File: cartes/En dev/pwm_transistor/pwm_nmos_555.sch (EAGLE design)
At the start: 15 parts, among them Q1 MOSFET-NCHANNELFQP30N06L, T1 2N2222

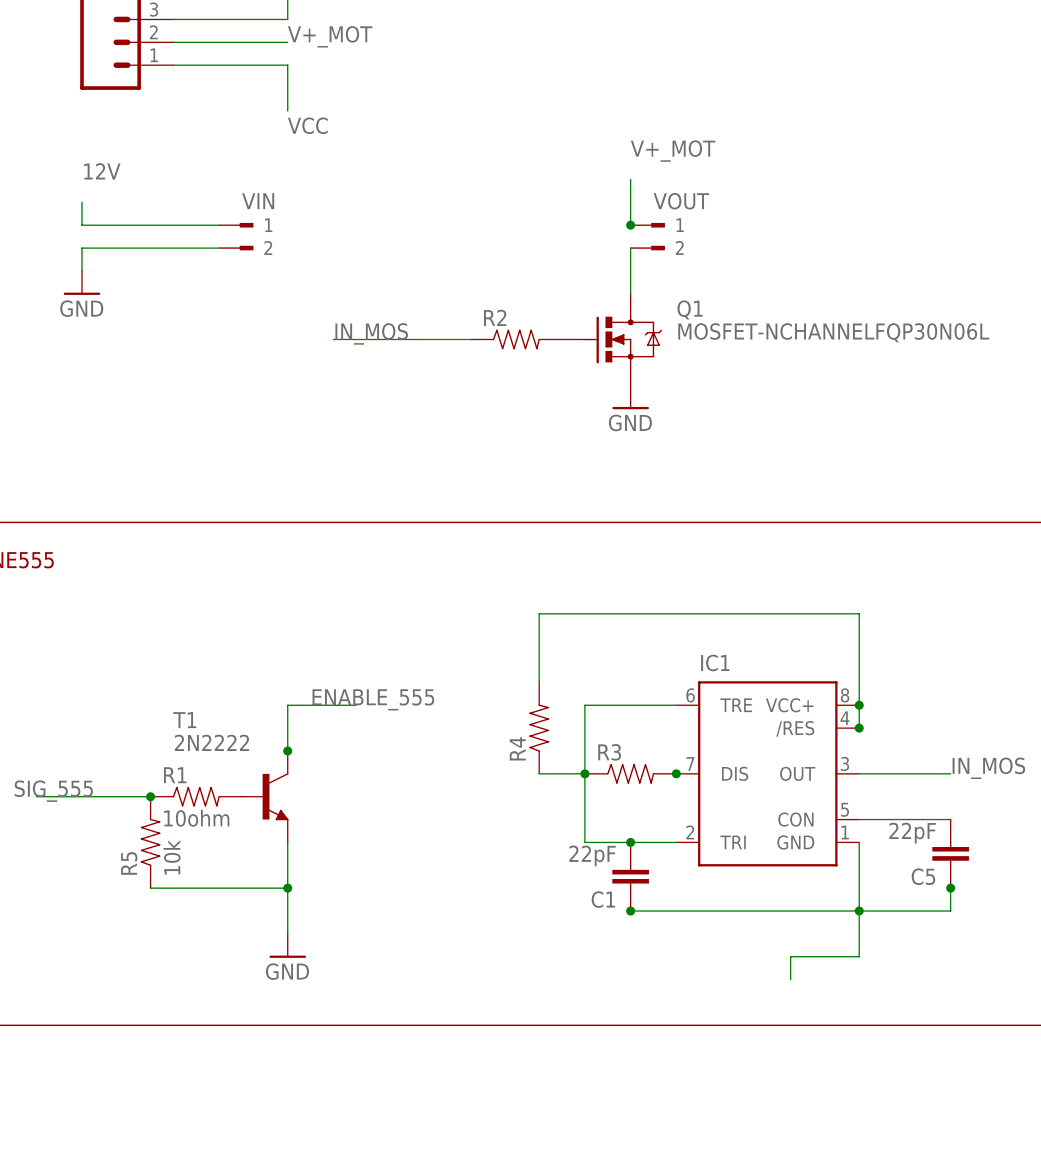
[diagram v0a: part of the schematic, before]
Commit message: carte mos pwm modifié
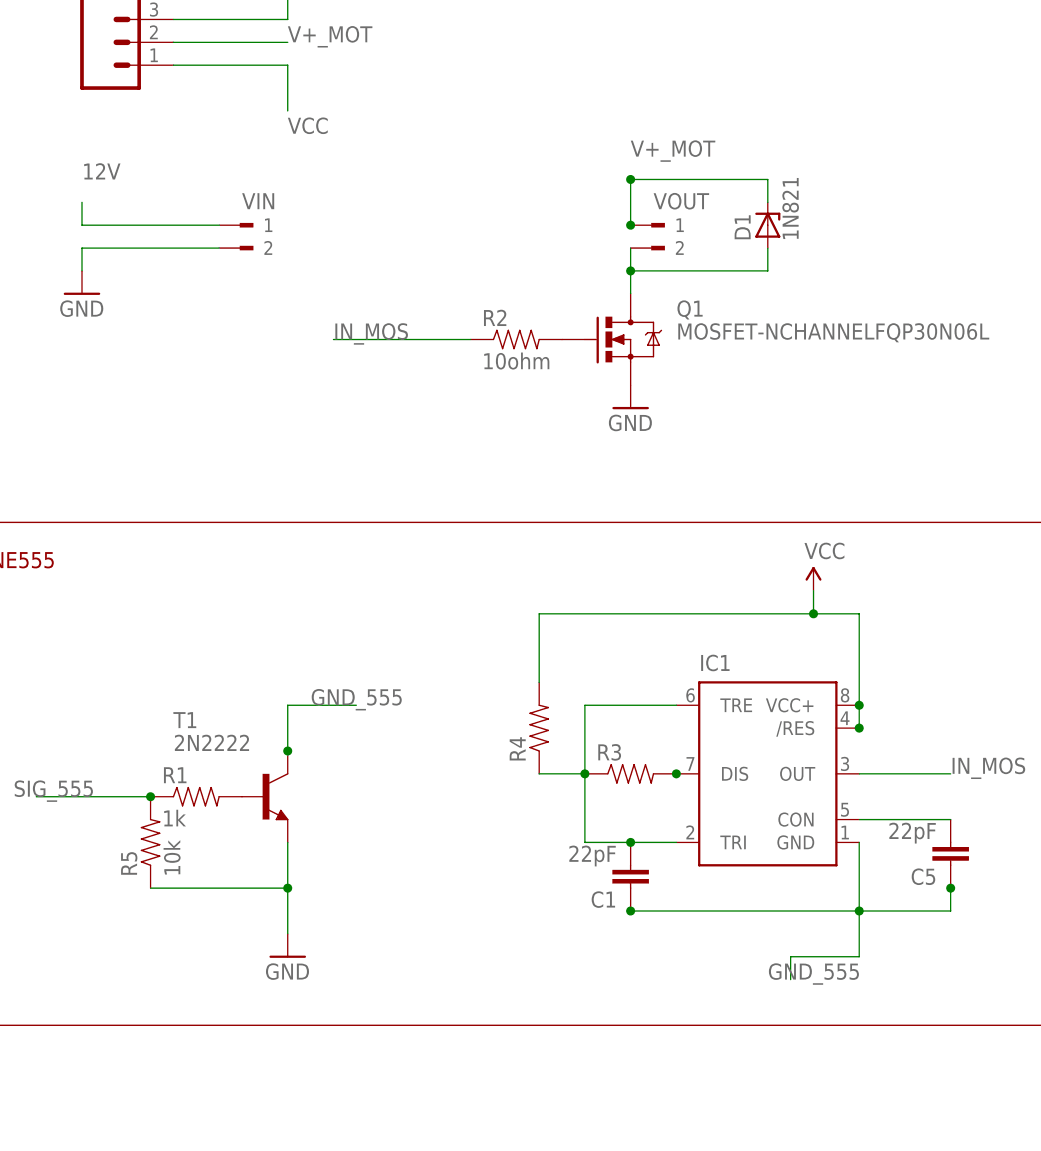
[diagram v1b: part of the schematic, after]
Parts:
- added D1: 1N821, diode:1N821
- R1: value 10ohm -> 1k
- R2: value (none) -> 10ohm
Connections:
- removed net ENABLE_555: T1.C
- removed net N$1: C1.1, C5.1, IC1.GND
- removed net N$7: IC1./RES, IC1.VCC+, R4.2
- new net GND_555: C1.1, C5.1, IC1.GND, T1.C
- net V+_MOT: now also D1.C
- net VCC: now also IC1./RES, IC1.VCC+, R4.2
- net VOUT: now also D1.A
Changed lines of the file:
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@@
 <part name="T1" library="adafruit" deviceset="2N2222" device=""/>
 <part name="INPUT" library="SparkFun-Electromechanical" deviceset="SMALL_SERVO" device="" value=""/>
-<part name="R1" library="SparkFun-Resistors" deviceset="RESISTOR" device="0805-RES" value="10ohm"/>
+<part name="R1" library="SparkFun-Resistors" deviceset="RESISTOR" device="0805-RES" value="1k"/>
 <part name="SUPPLY1" library="SparkFun-Aesthetics" deviceset="VCC" device=""/>
 <part name="GND1" library="SparkFun-Aesthetics" deviceset="GND" device=""/>
@@
 <part name="VIN" library="con-weidmueller-sl35" deviceset="90-2" device=""/>
 <part name="GND5" library="SparkFun-Aesthetics" deviceset="GND" device=""/>
-<part name="R2" library="SparkFun-Resistors" deviceset="RESISTOR" device="0805-RES"/>
+<part name="R2" library="SparkFun-Resistors" deviceset="RESISTOR" device="0805-RES" value="10ohm"/>
 <part name="SIGNAL" library="SparkFun-Connectors" deviceset="M03" device="PTH"/>
 <part name="R3" library="SparkFun-Resistors" deviceset="RESISTOR" device="0805-RES"/>
@@
 <part name="R5" library="SparkFun-Resistors" deviceset="RESISTOR" device="0805-RES" value="10k"/>
 <part name="V_MOT" library="SparkFun-Connectors" deviceset="M03" device="PTH"/>
+<part name="SUPPLY2" library="SparkFun-Aesthetics" deviceset="VCC" device=""/>
+<part name="D1" library="diode" deviceset="1N821" device=""/>
 </parts>
 <sheets>
@@
 <instance part="R5" gate="G$1" x="-88.9" y="-43.18" rot="R90"/>
 <instance part="V_MOT" gate="G$1" x="-93.98" y="45.72"/>
+<instance part="SUPPLY2" gate="1" x="-15.24" y="-15.24"/>
+<instance part="D1" gate="1" x="-20.32" y="25.4" rot="R90"/>
 </instances>
 <busses>
@@
 <label x="-73.66" y="35.56" size="1.778" layer="95"/>
 </segment>
-</net>
-<net name="ENABLE_555" class="0">
-<segment>
-<pinref part="T1" gate="G$1" pin="C"/>
-<wire x1="-73.66" y1="-33.02" x2="-73.66" y2="-27.94" width="0.1524" layer="91"/>
-<wire x1="-73.66" y1="-27.94" x2="-66.04" y2="-27.94" width="0.1524" layer="91"/>
-<label x="-71.12" y="-27.94" size="1.778" layer="95"/>
-<junction x="-73.66" y="-33.02"/>
+<segment>
+<pinref part="IC1" gate="G$1" pin="/RES"/>
+<pinref part="IC1" gate="G$1" pin="VCC+"/>
+<wire x1="-10.16" y1="-27.94" x2="-10.16" y2="-30.48" width="0.1524" layer="91"/>
+<wire x1="-45.72" y1="-17.78" x2="-15.24" y2="-17.78" width="0.1524" layer="91"/>
+<wire x1="-15.24" y1="-17.78" x2="-10.16" y2="-17.78" width="0.1524" layer="91"/>
+<wire x1="-10.16" y1="-17.78" x2="-10.16" y2="-27.94" width="0.1524" layer="91"/>
+<pinref part="R4" gate="G$1" pin="2"/>
+<wire x1="-45.72" y1="-17.78" x2="-45.72" y2="-25.4" width="0.1524" layer="91"/>
+<junction x="-10.16" y="-27.94"/>
+<junction x="-10.16" y="-30.48"/>
+<junction x="-15.24" y="-17.78"/>
+<wire x1="-15.24" y1="-17.78" x2="-15.24" y2="-15.24" width="0.1524" layer="91"/>
+<pinref part="SUPPLY2" gate="1" pin="VCC"/>
 </segment>
 </net>
@@
 <segment>
 <pinref part="Q1" gate="G$1" pin="D"/>
-<wire x1="-35.56" y1="22.86" x2="-35.56" y2="17.78" width="0.1524" layer="91"/>
+<wire x1="-35.56" y1="22.86" x2="-35.56" y2="20.32" width="0.1524" layer="91"/>
 <pinref part="VOUT" gate="G$1" pin="2"/>
+<pinref part="D1" gate="1" pin="A"/>
+<wire x1="-35.56" y1="20.32" x2="-35.56" y2="17.78" width="0.1524" layer="91"/>
+<wire x1="-35.56" y1="20.32" x2="-20.32" y2="20.32" width="0.1524" layer="91"/>
+<wire x1="-20.32" y1="20.32" x2="-20.32" y2="22.86" width="0.1524" layer="91"/>
+<junction x="-35.56" y="20.32"/>
 </segment>
 </net>
@@
 </segment>
 </net>
-<net name="N$7" class="0">
-<segment>
-<pinref part="IC1" gate="G$1" pin="/RES"/>
-<pinref part="IC1" gate="G$1" pin="VCC+"/>
-<wire x1="-10.16" y1="-27.94" x2="-10.16" y2="-30.48" width="0.1524" layer="91"/>
-<wire x1="-45.72" y1="-17.78" x2="-10.16" y2="-17.78" width="0.1524" layer="91"/>
-<wire x1="-10.16" y1="-17.78" x2="-10.16" y2="-27.94" width="0.1524" layer="91"/>
-<pinref part="R4" gate="G$1" pin="2"/>
-<wire x1="-45.72" y1="-17.78" x2="-45.72" y2="-25.4" width="0.1524" layer="91"/>
-<junction x="-10.16" y="-27.94"/>
-<junction x="-10.16" y="-30.48"/>
-</segment>
-</net>
 <net name="N$8" class="0">
 <segment>
@@
 <label x="-35.56" y="33.02" size="1.778" layer="95"/>
 <junction x="-35.56" y="25.4"/>
+<pinref part="D1" gate="1" pin="C"/>
+<wire x1="-35.56" y1="30.48" x2="-20.32" y2="30.48" width="0.1524" layer="91"/>
+<wire x1="-20.32" y1="30.48" x2="-20.32" y2="27.94" width="0.1524" layer="91"/>
+<junction x="-35.56" y="30.48"/>
 </segment>
 <segment>
@@
 </segment>
 </net>
-<net name="N$1" class="0">
+<net name="GND_555" class="0">
+<segment>
+<pinref part="T1" gate="G$1" pin="C"/>
+<wire x1="-73.66" y1="-33.02" x2="-73.66" y2="-27.94" width="0.1524" layer="91"/>
+<wire x1="-73.66" y1="-27.94" x2="-66.04" y2="-27.94" width="0.1524" layer="91"/>
+<label x="-71.12" y="-27.94" size="1.778" layer="95"/>
+<junction x="-73.66" y="-33.02"/>
+</segment>
 <segment>
 <pinref part="IC1" gate="G$1" pin="GND"/>
@@
 <wire x1="-10.16" y1="-55.88" x2="-17.78" y2="-55.88" width="0.1524" layer="91"/>
 <wire x1="-17.78" y1="-55.88" x2="-17.78" y2="-58.42" width="0.1524" layer="91"/>
-</segment>
-</net>
+<label x="-20.32" y="-58.42" size="1.778" layer="95"/>
+</segment>
+</net>
